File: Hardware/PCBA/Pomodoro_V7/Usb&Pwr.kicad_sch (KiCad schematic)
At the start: 12 parts, among them J4 USB4120-03-C_REVA, J9 Conn_01x02_Pin, U2 USBLC6-2SC6, U3 AP2112K-3.3

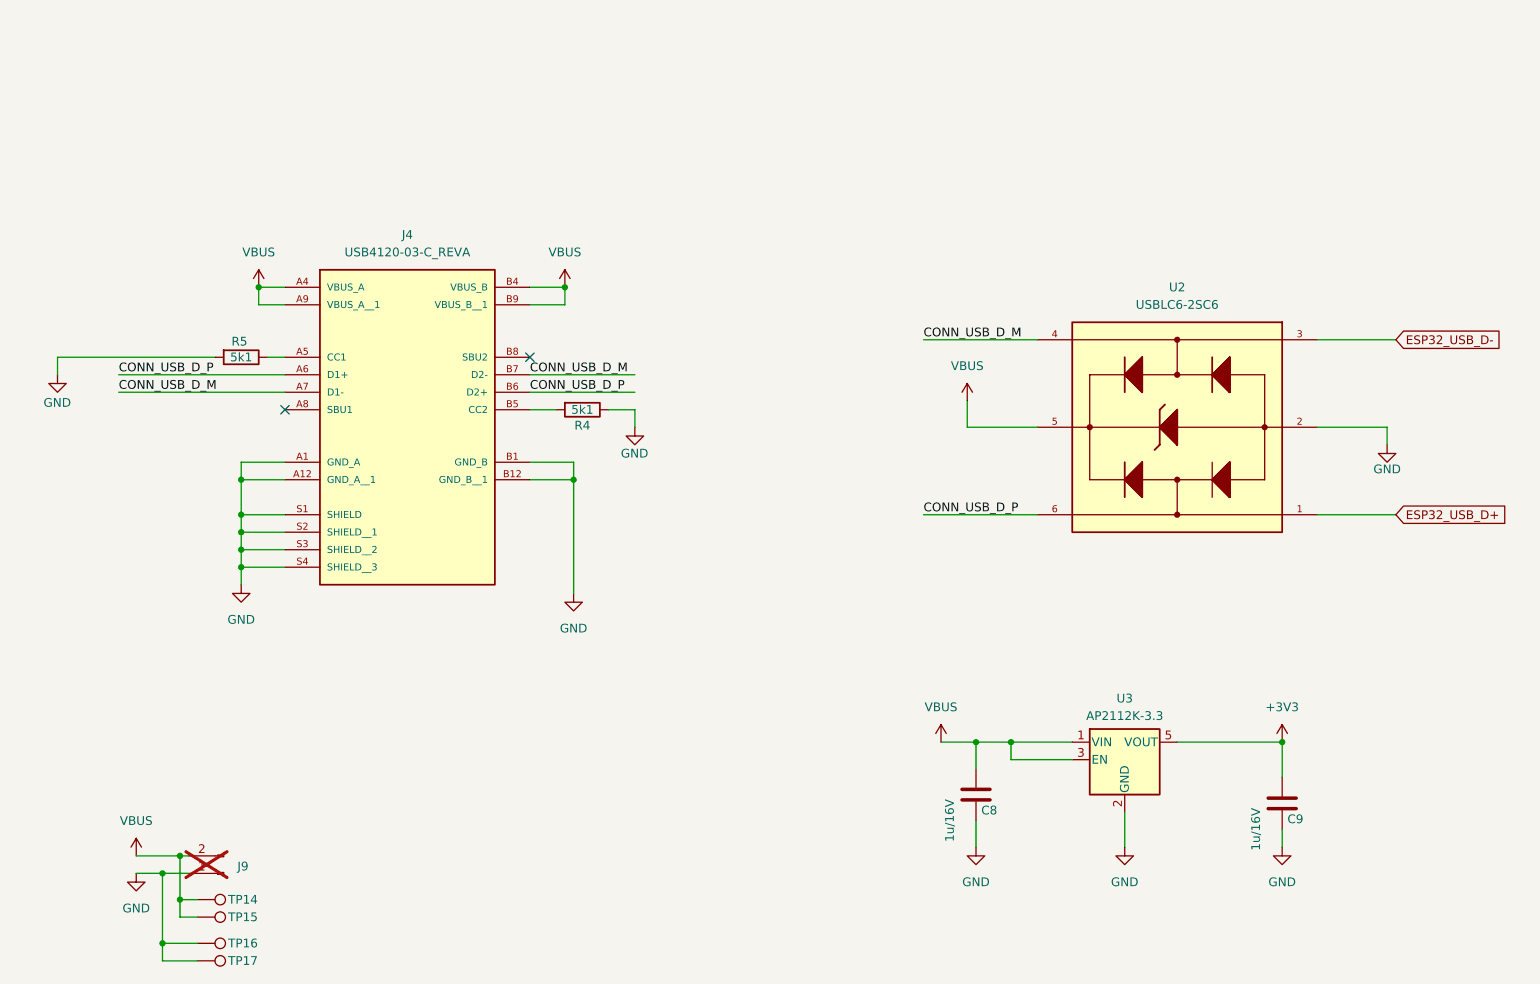
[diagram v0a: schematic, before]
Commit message: FW can now be flashed to an ESP32-S2 Target; Completed the Schematic
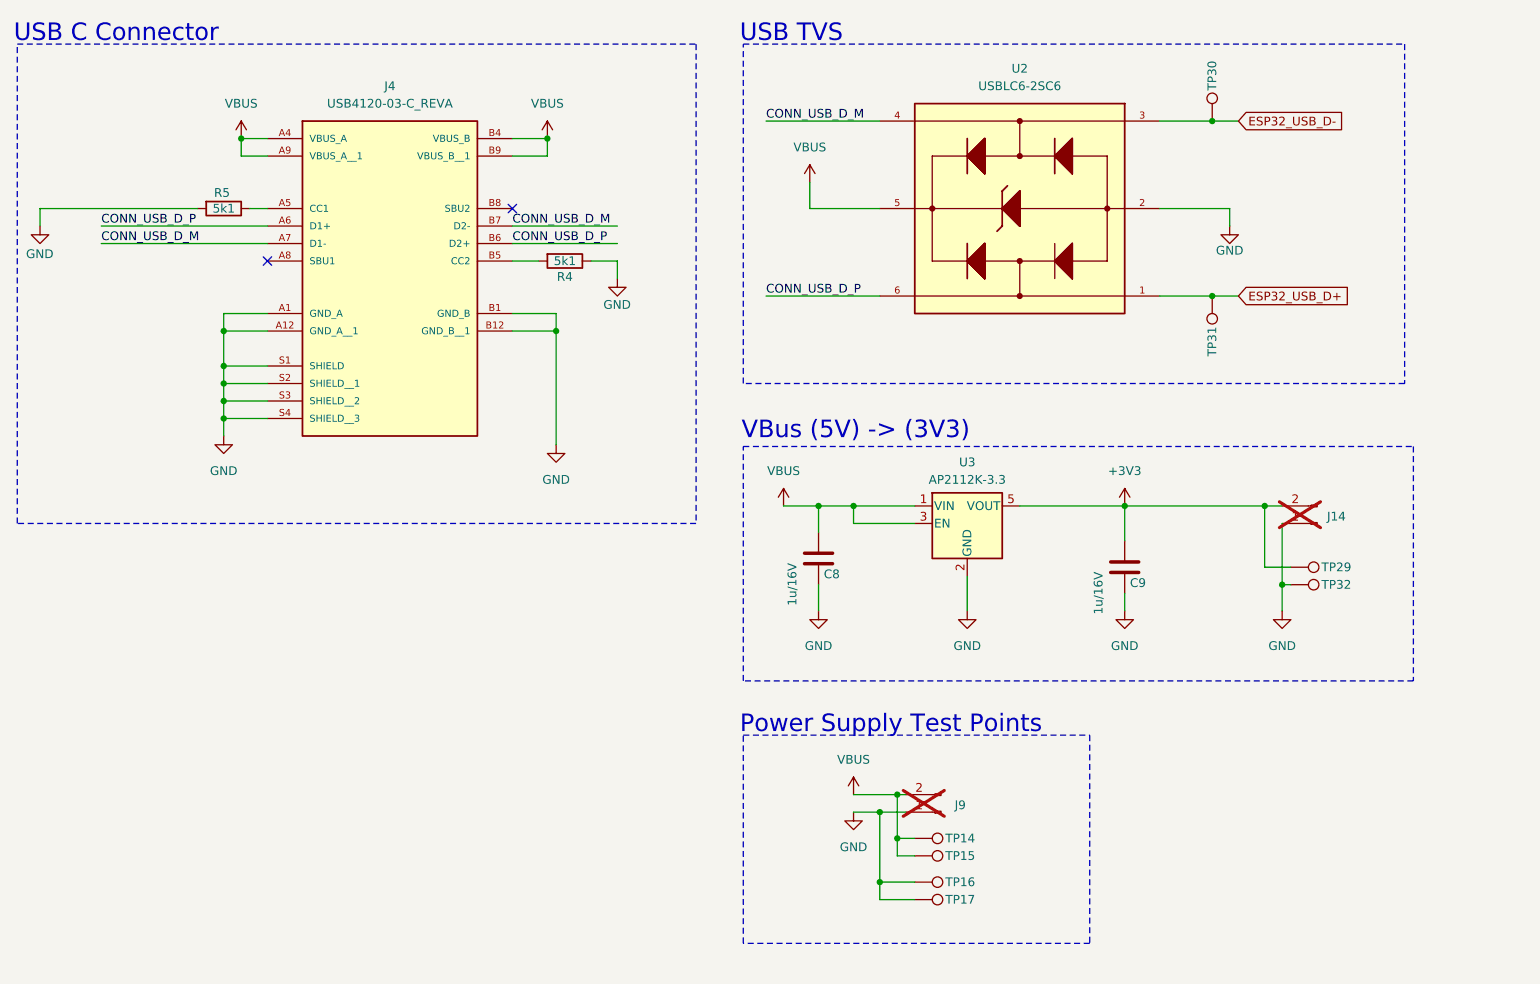
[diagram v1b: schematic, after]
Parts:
- added J14: Conn_01x02_Pin, Connector_PinHeader_2.54mm:PinHeader_1x02_P2.54mm_Vertical, symbol Connector:Conn_01x02_Pin
- added TP29, TP30, TP31, TP32: TestPoint, TestPoint:TestPoint_Pad_D1.0mm, symbol Connector:TestPoint
- J9: footprint (none) -> Connector_PinHeader_2.54mm:PinHeader_1x02_P2.54mm_Vertical
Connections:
- net +3V3: now also J14.2 (Pin_2), TP29.1
- net ESP32_USB_D+: now also TP31.1
- net ESP32_USB_D-: now also TP30.1
- net GND: now also J14.1 (Pin_1), TP32.1
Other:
- note added: "Power Supply Test Points"
- note added: "USB C Connector"
- note added: "USB TVS"
- note added: "VBus (5V) -> (3V3)"
- moved on the sheet: C8, C9, J4, R4, R5, TP14, TP15, TP16, TP17, U2, U3

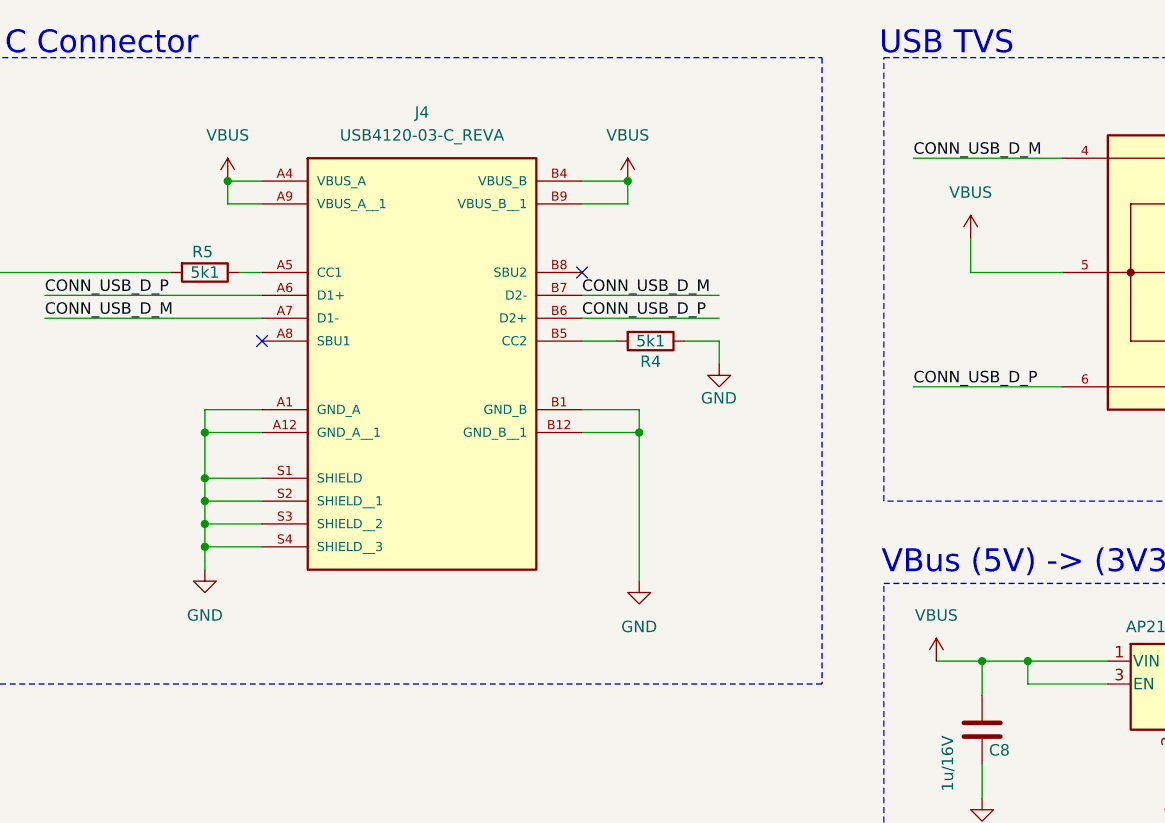
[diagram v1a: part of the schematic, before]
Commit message: added the selector wheel, changed the Connectors on the Trigger Button to move the assemlby closer together
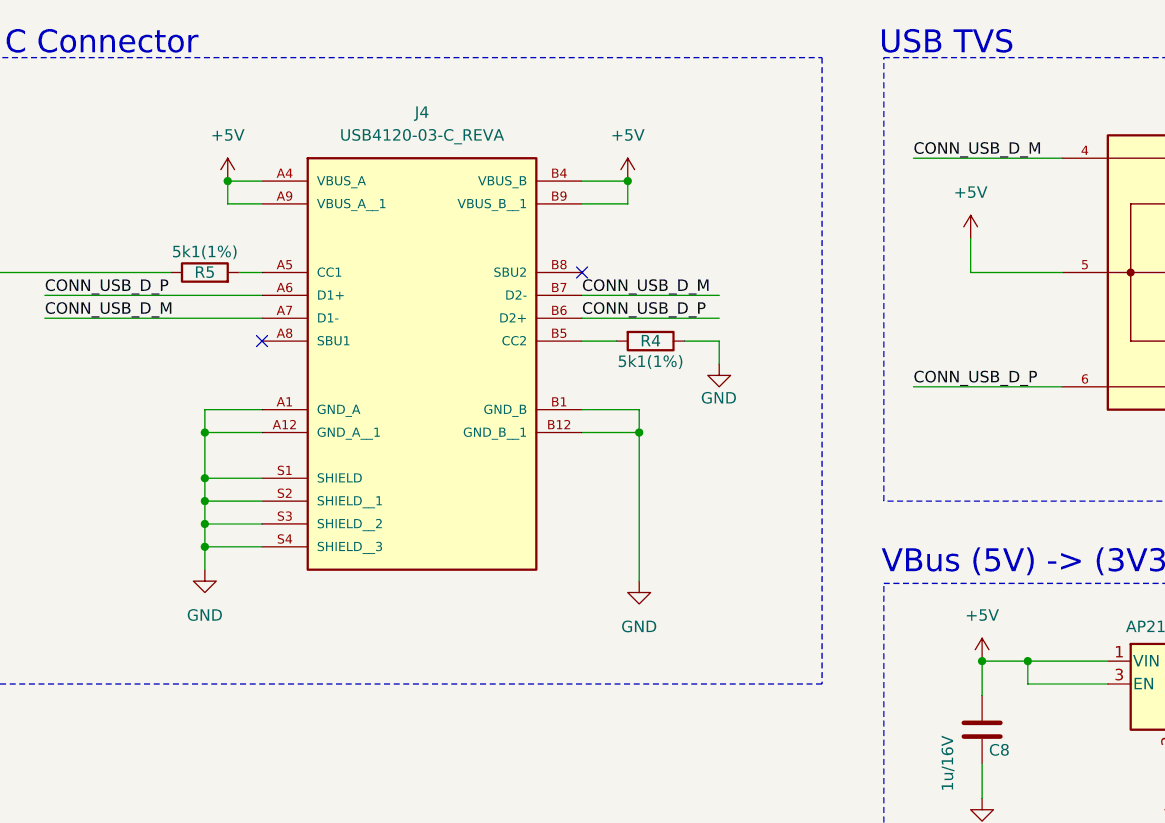
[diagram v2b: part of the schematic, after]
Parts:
- R4, R5: value 5k1 -> 5k1(1%); MPN (none) -> CR0805-FX-5101ELF; Part ID (none) -> CR0805-FX-5101ELF
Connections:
- net GND: now also R5.1; no longer R5.2
- net VBUS: no longer C8.1, J4.A4 (VBUS_A), J4.A9 (VBUS_A__1), J4.B4 (VBUS_B), J4.B9 (VBUS_B__1), U2.5, U3.1 (VIN), U3.3 (EN)
- net at J4.A5 (CC1): now also R5.2; no longer R5.1
- new net +5V: C8.1, J4.A4 (VBUS_A), J4.A9 (VBUS_A__1), J4.B4 (VBUS_B), J4.B9 (VBUS_B__1), U2.5, U3.1 (VIN), U3.3 (EN)

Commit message: Update on the PCBA
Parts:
- renumbered J4 to J11, J14 to J12, J9 to J13, R4 to R10, R5 to R9, TP30 to TP26, TP31 to TP27, TP29 to TP28, TP32 to TP29, TP14 to TP30, TP15 to TP31, TP16 to TP32, TP17 to TP33
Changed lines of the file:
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@@
 		(on_board yes)
 		(dnp no)
-		(property "Reference" "TP32"
+		(property "Reference" "TP29"
 			(at 208.534 97.79 90)
 			(effects
@@
 			(project "Pomodoro_V7"
 				(path "/7b50fc13-bee1-48b7-8eab-d6ef36855383/1961c4fe-101c-4224-bef0-a37787d4c52f"
-					(reference "TP32")
+					(reference "TP29")
 					(unit 1)
 				)
@@
 		(on_board yes)
 		(dnp no)
-		(property "Reference" "TP14"
+		(property "Reference" "TP30"
 			(at 153.924 134.62 90)
 			(effects
@@
 			(project "Pomodoro_V7"
 				(path "/7b50fc13-bee1-48b7-8eab-d6ef36855383/1961c4fe-101c-4224-bef0-a37787d4c52f"
-					(reference "TP14")
+					(reference "TP30")
 					(unit 1)
 				)
@@
 		(dnp no)
 		(fields_autoplaced yes)
-		(property "Reference" "#PWR037"
+		(property "Reference" "#PWR034"
 			(at 93.98 36.83 0)
 			(effects
@@
 			(project "Pomodoro_V7"
 				(path "/7b50fc13-bee1-48b7-8eab-d6ef36855383/1961c4fe-101c-4224-bef0-a37787d4c52f"
-					(reference "#PWR037")
+					(reference "#PWR034")
 					(unit 1)
 				)
@@
 		(dnp no)
 		(fields_autoplaced yes)
-		(property "Reference" "#PWR039"
+		(property "Reference" "#PWR047"
 			(at 138.43 132.08 0)
 			(effects
@@
 			(project "Pomodoro_V7"
 				(path "/7b50fc13-bee1-48b7-8eab-d6ef36855383/1961c4fe-101c-4224-bef0-a37787d4c52f"
-					(reference "#PWR039")
+					(reference "#PWR047")
 					(unit 1)
 				)
@@
 		(dnp no)
 		(fields_autoplaced yes)
-		(property "Reference" "#PWR054"
+		(property "Reference" "#PWR043"
 			(at 133.35 107.95 0)
 			(effects
@@
 			(project "Pomodoro_V7"
 				(path "/7b50fc13-bee1-48b7-8eab-d6ef36855383/1961c4fe-101c-4224-bef0-a37787d4c52f"
-					(reference "#PWR054")
+					(reference "#PWR043")
 					(unit 1)
 				)
@@
 		(dnp no)
 		(fields_autoplaced yes)
-		(property "Reference" "#PWR058"
+		(property "Reference" "#PWR041"
 			(at 133.35 90.17 0)
 			(effects
@@
 			(project "Pomodoro_V7"
 				(path "/7b50fc13-bee1-48b7-8eab-d6ef36855383/1961c4fe-101c-4224-bef0-a37787d4c52f"
-					(reference "#PWR058")
+					(reference "#PWR041")
 					(unit 1)
 				)
@@
 		(on_board yes)
 		(dnp no)
-		(property "Reference" "#PWR050"
+		(property "Reference" "#PWR037"
 			(at 193.04 52.07 0)
 			(effects
@@
 			(project "Pomodoro_V7"
 				(path "/7b50fc13-bee1-48b7-8eab-d6ef36855383/1961c4fe-101c-4224-bef0-a37787d4c52f"
-					(reference "#PWR050")
+					(reference "#PWR037")
 					(unit 1)
 				)
@@
 		(on_board yes)
 		(dnp no)
-		(property "Reference" "TP16"
+		(property "Reference" "TP32"
 			(at 153.924 140.97 90)
 			(effects
@@
 			(project "Pomodoro_V7"
 				(path "/7b50fc13-bee1-48b7-8eab-d6ef36855383/1961c4fe-101c-4224-bef0-a37787d4c52f"
-					(reference "TP16")
+					(reference "TP32")
 					(unit 1)
 				)
@@
 		(on_board yes)
 		(dnp no)
-		(property "Reference" "TP29"
+		(property "Reference" "TP28"
 			(at 208.534 95.25 90)
 			(effects
@@
 			(project "Pomodoro_V7"
 				(path "/7b50fc13-bee1-48b7-8eab-d6ef36855383/1961c4fe-101c-4224-bef0-a37787d4c52f"
-					(reference "TP29")
+					(reference "TP28")
 					(unit 1)
 				)
@@
 		(dnp no)
 		(fields_autoplaced yes)
-		(property "Reference" "#PWR032"
+		(property "Reference" "#PWR040"
 			(at 95.25 83.82 0)
 			(effects
@@
 			(project "Pomodoro_V7"
 				(path "/7b50fc13-bee1-48b7-8eab-d6ef36855383/1961c4fe-101c-4224-bef0-a37787d4c52f"
-					(reference "#PWR032")
+					(reference "#PWR040")
 					(unit 1)
 				)
@@
 		(dnp no)
 		(fields_autoplaced yes)
-		(property "Reference" "#PWR031"
+		(property "Reference" "#PWR039"
 			(at 46.99 82.55 0)
 			(effects
@@
 			(project "Pomodoro_V7"
 				(path "/7b50fc13-bee1-48b7-8eab-d6ef36855383/1961c4fe-101c-4224-bef0-a37787d4c52f"
-					(reference "#PWR031")
+					(reference "#PWR039")
 					(unit 1)
 				)
@@
 		(on_board yes)
 		(dnp no)
-		(property "Reference" "TP30"
+		(property "Reference" "TP26"
 			(at 190.5 23.876 90)
 			(effects
@@
 			(project "Pomodoro_V7"
 				(path "/7b50fc13-bee1-48b7-8eab-d6ef36855383/1961c4fe-101c-4224-bef0-a37787d4c52f"
-					(reference "TP30")
+					(reference "TP26")
 					(unit 1)
 				)
@@
 		(dnp no)
 		(fields_autoplaced yes)
-		(property "Reference" "#PWR051"
+		(property "Reference" "#PWR033"
 			(at 49.53 36.83 0)
 			(effects
@@
 			(project "Pomodoro_V7"
 				(path "/7b50fc13-bee1-48b7-8eab-d6ef36855383/1961c4fe-101c-4224-bef0-a37787d4c52f"
-					(reference "#PWR051")
+					(reference "#PWR033")
 					(unit 1)
 				)
@@
 		(dnp no)
 		(fields_autoplaced yes)
-		(property "Reference" "J4"
+		(property "Reference" "J11"
 			(at 71.12 25.4 0)
 			(effects
@@
 			(project "Pomodoro_V7"
 				(path "/7b50fc13-bee1-48b7-8eab-d6ef36855383/1961c4fe-101c-4224-bef0-a37787d4c52f"
-					(reference "J4")
+					(reference "J11")
 					(unit 1)
 				)
@@
 		(dnp no)
 		(fields_autoplaced yes)
-		(property "Reference" "#PWR055"
+		(property "Reference" "#PWR044"
 			(at 154.94 107.95 0)
 			(effects
@@
 			(project "Pomodoro_V7"
 				(path "/7b50fc13-bee1-48b7-8eab-d6ef36855383/1961c4fe-101c-4224-bef0-a37787d4c52f"
-					(reference "#PWR055")
+					(reference "#PWR044")
 					(unit 1)
 				)
@@
 		(dnp no)
 		(fields_autoplaced yes)
-		(property "Reference" "#PWR047"
+		(property "Reference" "#PWR048"
 			(at 138.43 137.16 0)
 			(effects
@@
 			(project "Pomodoro_V7"
 				(path "/7b50fc13-bee1-48b7-8eab-d6ef36855383/1961c4fe-101c-4224-bef0-a37787d4c52f"
-					(reference "#PWR047")
+					(reference "#PWR048")
 					(unit 1)
 				)
@@
 		(dnp no)
 		(fields_autoplaced yes)
-		(property "Reference" "#PWR053"
+		(property "Reference" "#PWR042"
 			(at 177.8 90.17 0)
 			(effects
@@
 			(project "Pomodoro_V7"
 				(path "/7b50fc13-bee1-48b7-8eab-d6ef36855383/1961c4fe-101c-4224-bef0-a37787d4c52f"
-					(reference "#PWR053")
+					(reference "#PWR042")
 					(unit 1)
 				)
@@
 		(on_board yes)
 		(dnp yes)
-		(property "Reference" "J14"
+		(property "Reference" "J12"
 			(at 208.534 87.884 0)
 			(effects
@@
 			(project "Pomodoro_V7"
 				(path "/7b50fc13-bee1-48b7-8eab-d6ef36855383/1961c4fe-101c-4224-bef0-a37787d4c52f"
-					(reference "J14")
+					(reference "J12")
 					(unit 1)
 				)
@@
 		(dnp no)
 		(fields_autoplaced yes)
-		(property "Reference" "#PWR036"
+		(property "Reference" "#PWR035"
 			(at 132.08 43.18 0)
 			(effects
@@
 			(project "Pomodoro_V7"
 				(path "/7b50fc13-bee1-48b7-8eab-d6ef36855383/1961c4fe-101c-4224-bef0-a37787d4c52f"
-					(reference "#PWR036")
+					(reference "#PWR035")
 					(unit 1)
 				)
@@
 		(on_board yes)
 		(dnp no)
-		(property "Reference" "R4"
+		(property "Reference" "R10"
 			(at 96.52 50.8 90)
 			(effects
@@
 			(project "Pomodoro_V7"
 				(path "/7b50fc13-bee1-48b7-8eab-d6ef36855383/1961c4fe-101c-4224-bef0-a37787d4c52f"
-					(reference "R4")
+					(reference "R10")
 					(unit 1)
 				)
@@
 		(on_board yes)
 		(dnp yes)
-		(property "Reference" "J9"
+		(property "Reference" "J13"
 			(at 153.924 129.794 0)
 			(effects
@@
 			(project "Pomodoro_V7"
 				(path "/7b50fc13-bee1-48b7-8eab-d6ef36855383/1961c4fe-101c-4224-bef0-a37787d4c52f"
-					(reference "J9")
+					(reference "J13")
 					(unit 1)
 				)
@@
 		(on_board yes)
 		(dnp no)
-		(property "Reference" "R5"
+		(property "Reference" "R9"
 			(at 46.99 43.18 90)
 			(effects
@@
 			(project "Pomodoro_V7"
 				(path "/7b50fc13-bee1-48b7-8eab-d6ef36855383/1961c4fe-101c-4224-bef0-a37787d4c52f"
-					(reference "R5")
+					(reference "R9")
 					(unit 1)
 				)
@@
 		(on_board yes)
 		(dnp no)
-		(property "Reference" "#PWR035"
+		(property "Reference" "#PWR036"
 			(at 20.32 52.07 0)
 			(effects
@@
 			(project "Pomodoro_V7"
 				(path "/7b50fc13-bee1-48b7-8eab-d6ef36855383/1961c4fe-101c-4224-bef0-a37787d4c52f"
-					(reference "#PWR035")
+					(reference "#PWR036")
 					(unit 1)
 				)
@@
 		(dnp no)
 		(fields_autoplaced yes)
-		(property "Reference" "#PWR057"
+		(property "Reference" "#PWR046"
 			(at 200.66 107.95 0)
 			(effects
@@
 			(project "Pomodoro_V7"
 				(path "/7b50fc13-bee1-48b7-8eab-d6ef36855383/1961c4fe-101c-4224-bef0-a37787d4c52f"
-					(reference "#PWR057")
+					(reference "#PWR046")
 					(unit 1)
 				)
@@
 		(dnp no)
 		(fields_autoplaced yes)
-		(property "Reference" "#PWR056"
+		(property "Reference" "#PWR045"
 			(at 177.8 107.95 0)
 			(effects
@@
 			(project "Pomodoro_V7"
 				(path "/7b50fc13-bee1-48b7-8eab-d6ef36855383/1961c4fe-101c-4224-bef0-a37787d4c52f"
-					(reference "#PWR056")
+					(reference "#PWR045")
 					(unit 1)
 				)
@@
 		(on_board yes)
 		(dnp no)
-		(property "Reference" "#PWR034"
+		(property "Reference" "#PWR038"
 			(at 104.14 59.69 0)
 			(effects
@@
 			(project "Pomodoro_V7"
 				(path "/7b50fc13-bee1-48b7-8eab-d6ef36855383/1961c4fe-101c-4224-bef0-a37787d4c52f"
-					(reference "#PWR034")
+					(reference "#PWR038")
 					(unit 1)
 				)
@@
 		(on_board yes)
 		(dnp no)
-		(property "Reference" "TP17"
+		(property "Reference" "TP33"
 			(at 153.924 143.51 90)
 			(effects
@@
 			(project "Pomodoro_V7"
 				(path "/7b50fc13-bee1-48b7-8eab-d6ef36855383/1961c4fe-101c-4224-bef0-a37787d4c52f"
-					(reference "TP17")
+					(reference "TP33")
 					(unit 1)
 				)
@@
 		(on_board yes)
 		(dnp no)
-		(property "Reference" "TP15"
+		(property "Reference" "TP31"
 			(at 153.924 137.16 90)
 			(effects
@@
 			(project "Pomodoro_V7"
 				(path "/7b50fc13-bee1-48b7-8eab-d6ef36855383/1961c4fe-101c-4224-bef0-a37787d4c52f"
-					(reference "TP15")
+					(reference "TP31")
 					(unit 1)
 				)
@@
 		(on_board yes)
 		(dnp no)
-		(property "Reference" "TP31"
+		(property "Reference" "TP27"
 			(at 190.5 62.484 90)
 			(effects
@@
 			(project "Pomodoro_V7"
 				(path "/7b50fc13-bee1-48b7-8eab-d6ef36855383/1961c4fe-101c-4224-bef0-a37787d4c52f"
-					(reference "TP31")
-					(unit 1)
-				)
+					(reference "TP27")
+					(unit 1)
+				)

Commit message: Completed the PCBA Design - the formal part
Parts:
- removed TP26, TP27: TestPoint, TestPoint:TestPoint_Pad_D1.0mm, symbol Connector:TestPoint
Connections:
- net VBUS is gone; now on net +5V: J13.2 (Pin_2), TP30.1, TP31.1
- net CONN_USB_D_M renamed CONN_USB_D-
- net CONN_USB_D-: now also U2.6; no longer U2.4
- net CONN_USB_D_P renamed CONN_USB_D+
- net CONN_USB_D+: now also U2.4; no longer U2.6

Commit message: Updated the PCBA Files
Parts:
- C8, C9: value 1u/16V -> 1u/16V+/X5R
- J11: Mfg Part # (none) -> USB4120-03-C
- TP28, TP29, TP30, TP31, TP32, TP33: now not fitted
- U2: Mfg Part # (none) -> USBLC6-2SC6
- U3: Mfg Part # (none) -> AP2112K-3.3TRG1
